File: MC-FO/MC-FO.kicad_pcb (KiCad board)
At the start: 4 copper layers, 160 x 100 mm, 93 parts, among them U101 74ACT08SCX, U102 IFE98, U121 74ACT08SCX, U122 IFE98, U141 IFD97, U142 TLV3501AID, U143 74LVC1G32SE-7, U161 IFD97, U163 74LVC1G32SE-7, U181 BU4831F-TR, U182 BU4847F-TR, U183 74ACT08SCX, U184 74LVC1G07QDCKTQ1, U2 R-78E3.3-0.5, U27 74ACT08SCX, U28 IFE98, U3 R-78E5.0-0.5, U41 74ACT08SCX, U42 IFE98, U61 74ACT08SCX, U62 IFE98, U81 74ACT08SCX, U82 IFE98

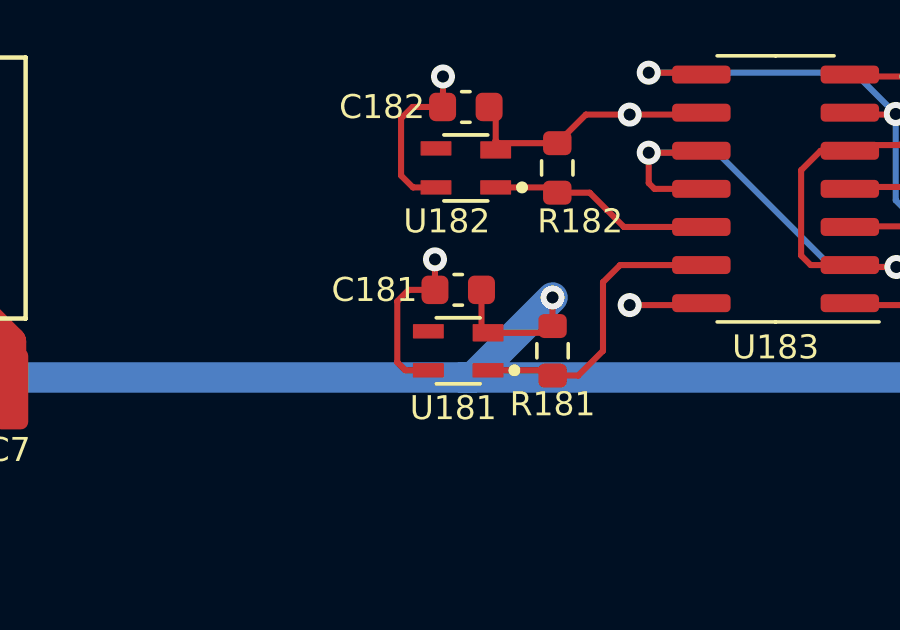
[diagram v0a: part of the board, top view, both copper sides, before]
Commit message: updated top level of schematic with "to test" and "to do" notes
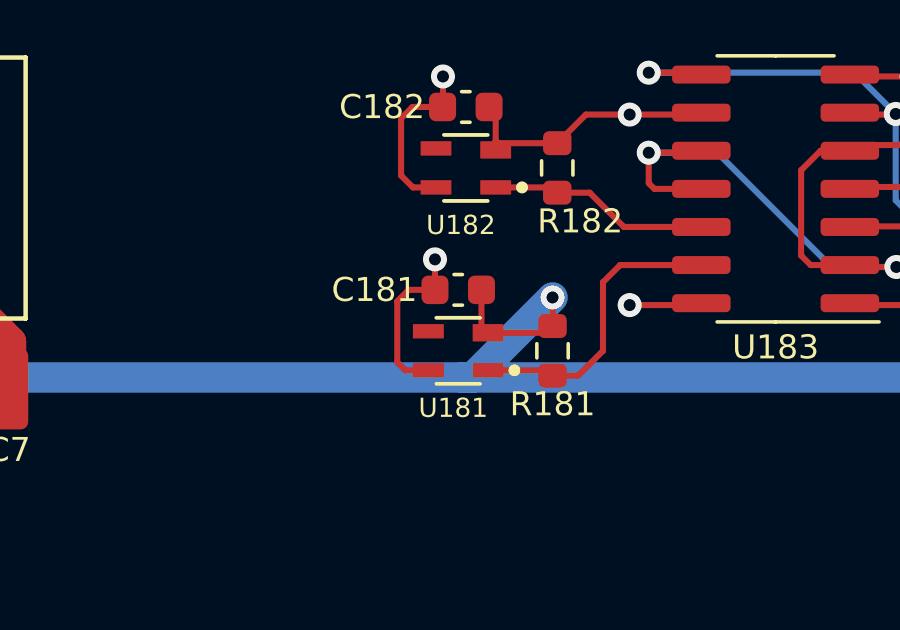
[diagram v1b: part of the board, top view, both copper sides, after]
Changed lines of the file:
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@@
   (general
     (thickness 1.6)
-    (drawings 20)
+    (drawings 30)
     (tracks 806)
     (zones 0)
@@
   (module BU4847F-TR:SOT130P210X105-4N (layer F.Cu)
     (at 168.275 66.802 180)
-    (fp_text reference U182 (at 0.635 -1.778) (layer F.SilkS)
-      (effects (font (size 0.8 0.8) (thickness 0.2)))
+    (fp_text reference U182 (at 0.167055 -1.907023) (layer F.SilkS)
+      (effects (font (size 0.640209 0.640209) (thickness 0.15)))
     )
-    (fp_text value BU4847F-TR (at 5.008681 1.881434) (layer F.Fab) hide
+    (fp_text value BU4847F-TR (at 5.008681 1.881434) (layer F.Fab)
       (effects (font (size 0.640624 0.640624) (thickness 0.15)))
     )
@@
     (at 168.021 72.898 180)
     (fp_text reference U181 (at 0.167055 -1.907023) (layer F.SilkS)
-      (effects (font (size 0.8 0.8) (thickness 0.2)))
+      (effects (font (size 0.640209 0.640209) (thickness 0.15)))
     )
-    (fp_text value BU4831F-TR (at 5.008681 1.881434) (layer F.Fab) hide
+    (fp_text value BU4831F-TR (at 5.008681 1.881434) (layer F.Fab)
       (effects (font (size 0.640624 0.640624) (thickness 0.15)))
     )
@@
     (pad 1 thru_hole circle (at 0 0 180) (size 1.445 1.445) (drill 0.889) (layers *.Cu *.Mask)
       (net 1 GND))
+    (model "C:/Program Files/KiCad/share/kicad/modules/LED_THT.pretty/LED_D2.0mm_W4.8mm_H2.5mm_FlatTop.kicad_mod"
+      (at (xyz 0 0 0))
+      (scale (xyz 1 1 1))
+      (rotate (xyz 0 0 0))
+    )
+    (model ${KISYS3DMOD}/LED_THT.3dshapes/LED_D5.0mm_Horizontal_O6.35mm_Z3.0mm.wrl
+      (offset (xyz 0 2.5 0))
+      (scale (xyz 1 1 1))
+      (rotate (xyz 0 0 90))
+    )
   )
   (module Capacitor_SMD:C_1210_3225Metric (layer F.Cu)
@@
     (pad 32 thru_hole circle (at 19.05 10.16 90) (size 1.55 1.55) (drill 1) (layers *.Cu *.Mask)
       (net 1 GND))
-    (model ${KISYS3DMOD}/Connector_DIN.3dshapes/DIN41612_C2_2x16_Male_Horizontal_THT.wrl
-      (at (xyz 0 0 0))
+    (model ${KISYS3DMOD}/Connector_Dsub.3dshapes/DSUB-25_Female_Horizontal_P2.77x2.84mm_EdgePinOffset7.70mm_Housed_MountingHolesOffset9.12mm.step
+      (offset (xyz -16.5 -10 0))
       (scale (xyz 1 1 1))
-      (rotate (xyz 0 0 0))
+      (rotate (xyz 0 0 180))
     )
   )
@@
     (pad 1 thru_hole circle (at 0 0 90) (size 1.1 1.1) (drill 0.7) (layers *.Cu *.Mask)
       (net 1 GND))
+    (model ${KIPRJMOD}/Footprints_MC-FO/FOport-IFE98-IFD97.STEP
+      (offset (xyz 1.9 -16.5 0))
+      (scale (xyz 1 1 1))
+      (rotate (xyz -90 0 -90))
+    )
   )
   (module Package_SO:SOIC-14_3.9x8.7mm_P1.27mm (layer F.Cu)
@@
     (pad 1 thru_hole circle (at 0 0 90) (size 1.1 1.1) (drill 0.7) (layers *.Cu *.Mask)
       (net 1 GND))
+    (model ${KIPRJMOD}/Footprints_MC-FO/FOport-IFE98-IFD97.STEP
+      (offset (xyz 1.9 -16.5 0))
+      (scale (xyz 1 1 1))
+      (rotate (xyz -90 0 -90))
+    )
   )
   (module Package_SO:SOIC-14_3.9x8.7mm_P1.27mm (layer F.Cu)
@@
     (pad MH2 np_thru_hole circle (at -0.635 2.54 90) (size 1.775 0) (drill 1.775) (layers *.Cu *.Mask))
     (pad MH3 np_thru_hole circle (at 4.445 2.54 90) (size 1.775 0) (drill 1.775) (layers *.Cu *.Mask))
+    (model ${KIPRJMOD}/Footprints_MC-FO/FOport-IFE98-IFD97.STEP
+      (offset (xyz 1.9 -16.5 0))
+      (scale (xyz 1 1 1))
+      (rotate (xyz -90 0 -90))
+    )
   )
   (module Package_SO:SOIC-14_3.9x8.7mm_P1.27mm (layer F.Cu)
@@
     (pad MH2 np_thru_hole circle (at -0.635 2.54 90) (size 1.775 0) (drill 1.775) (layers *.Cu *.Mask))
     (pad MH3 np_thru_hole circle (at 4.445 2.54 90) (size 1.775 0) (drill 1.775) (layers *.Cu *.Mask))
+    (model ${KIPRJMOD}/Footprints_MC-FO/FOport-IFE98-IFD97.STEP
+      (offset (xyz 1.9 -16.5 0))
+      (scale (xyz 1 1 1))
+      (rotate (xyz -90 0 -90))
+    )
   )
   (module Package_SO:SOIC-14_3.9x8.7mm_P1.27mm (layer F.Cu)
@@
     (pad MH2 np_thru_hole circle (at -0.635 2.54 90) (size 1.775 0) (drill 1.775) (layers *.Cu *.Mask))
     (pad MH3 np_thru_hole circle (at 4.445 2.54 90) (size 1.775 0) (drill 1.775) (layers *.Cu *.Mask))
+    (model ${KIPRJMOD}/Footprints_MC-FO/FOport-IFE98-IFD97.STEP
+      (offset (xyz 1.9 -16.5 0))
+      (scale (xyz 1 1 1))
+      (rotate (xyz -90 0 -90))
+    )
   )
   (module Package_SO:SOIC-14_3.9x8.7mm_P1.27mm (layer F.Cu)
@@
     (pad MH2 np_thru_hole circle (at -0.635 2.54 90) (size 1.775 0) (drill 1.775) (layers *.Cu *.Mask))
     (pad MH3 np_thru_hole circle (at 4.445 2.54 90) (size 1.775 0) (drill 1.775) (layers *.Cu *.Mask))
+    (model ${KIPRJMOD}/Footprints_MC-FO/FOport-IFE98-IFD97.STEP
+      (offset (xyz 1.9 -16.5 0))
+      (scale (xyz 1 1 1))
+      (rotate (xyz -90 0 -90))
+    )
   )
   (module Footprints_MC-FO:IFE98 locked (layer F.Cu)
@@
     (pad 1 thru_hole circle (at 0 0 90) (size 1.1 1.1) (drill 0.7) (layers *.Cu *.Mask)
       (net 4 /Detector1/5V))
+    (model ${KIPRJMOD}/Footprints_MC-FO/FOport-IFE98-IFD97.STEP
+      (offset (xyz 1.9 -16.5 0))
+      (scale (xyz 1 1 1))
+      (rotate (xyz -90 0 -90))
+    )
   )
   (module Package_SO:SOIC-8_3.9x4.9mm_P1.27mm (layer F.Cu)
@@
     (pad MH2 np_thru_hole circle (at -0.635 2.54 90) (size 1.775 0) (drill 1.775) (layers *.Cu *.Mask))
     (pad MH3 np_thru_hole circle (at 4.445 2.54 90) (size 1.775 0) (drill 1.775) (layers *.Cu *.Mask))
+    (model ${KIPRJMOD}/Footprints_MC-FO/FOport-IFE98-IFD97.STEP
+      (offset (xyz 1.9 -16.5 0))
+      (scale (xyz 1 1 1))
+      (rotate (xyz -90 0 -90))
+    )
   )
   (module Package_TO_SOT_SMD:SOT-353_SC-70-5 (layer F.Cu)
@@
     )
   )
+  (gr_line (start 211.582 100.965) (end 209.931 98.552) (layer Cmts.User) (width 0.15))
+  (gr_line (start 210.566 97.79) (end 210.82 98.806) (layer Cmts.User) (width 0.15))
+  (gr_line (start 212.217 98.425) (end 210.947 97.282) (layer Cmts.User) (width 0.15))
+  (gr_line (start 219.329 99.187) (end 217.17 97.155) (layer Cmts.User) (width 0.15))
+  (gr_line (start 218.313 97.663) (end 218.567 96.393) (layer Cmts.User) (width 0.15))
+  (gr_line (start 218.694 99.314) (end 219.202 100.076) (layer Cmts.User) (width 0.15))
+  (gr_line (start 218.567 101.219) (end 218.313 100.711) (layer Cmts.User) (width 0.15))
+  (gr_line (start 220.726 101.092) (end 217.424 99.822) (layer Cmts.User) (width 0.15))
+  (gr_line (start 217.297 102.743) (end 220.726 102.743) (layer Cmts.User) (width 0.15))
+  (gr_line (start 216.662 101.727) (end 218.059 101.854) (layer Cmts.User) (width 0.15))
   (gr_text "EPWMA1\n" (at 224.608 78.451571) (layer B.SilkS)
     (effects (font (size 1 1) (thickness 0.15)))

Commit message: Add files via upload
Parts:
- removed C144: 0.1 uF, Capacitor_SMD:C_0603_1608Metric
- removed R144: 47K, Resistor_SMD:R_0603_1608Metric
- removed U143, U163: 74LVC1G32SE-7, Package_TO_SOT_SMD:SOT-353_SC-70-5
- added U162: 74LVC1G02SE-7, Package_TO_SOT_SMD:SOT-353_SC-70-5, F.Cu at (221.4, 142.1)
- R142: value 1K -> 47K
- U142: value TLV3501AID -> 74LVC1G02SE-7; footprint Package_SO:SOIC-8_3.9x4.9mm_P1.27mm -> Package_TO_SOT_SMD:SOT-353_SC-70-5
- U181, U182: footprint BU4847F-TR:SOT130P210X105-4N -> Package_SO:SOP-4_3.8x4.1mm_P2.54mm
- moved R143 59.7 mm to (263.7, 100.4)
- moved R141 53.7 mm to (275.3, 100.1), turned to 90 degrees
- moved R142 52.0 mm to (273.6, 100.1), turned to 90 degrees
- moved U142 51.5 mm to (266.3, 100.3), turned to 270 degrees
- moved C143 49.6 mm to (268.9, 100.2), turned to 90 degrees
- moved C141 47.4 mm to (279.5, 100.3), turned to 90 degrees
- moved C142 47.0 mm to (279.1, 97.3), turned to 270 degrees
- moved R161 4.27 mm to (229.4, 144.0), turned to 90 degrees
- moved C161 3.00 mm to (231.5, 141.2)
- moved C162 3.00 mm to (231.5, 138.4)
- moved R162 1.74 mm to (227.3, 143.2), turned to 0 degrees
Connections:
- C101 pad 1: /Detector1/5V -> /Emitter1/5V
- C102 pad 1: /Detector1/5V -> /Emitter1/5V
- C103 pad 1: /Detector1/5V -> /Emitter1/5V
- C121 pad 1: /Detector1/5V -> /Emitter1/5V
- C122 pad 1: /Detector1/5V -> /Emitter1/5V
- C123 pad 1: /Detector1/5V -> /Emitter1/5V
- C141 pad 1: /Detector1/5V -> /Emitter1/5V
- C141 pad 2: GND -> Net-(C141-Pad2)
- C142 pad 1: /Detector1/5V -> /Emitter1/5V
- C142 pad 2: GND -> Net-(C141-Pad2)
- C143 pad 1: /Detector1/5V -> VCC
- C143 pad 2: GND -> Net-(C141-Pad2)
- C161 pad 1: /Detector1/5V -> /Emitter1/5V
- C162 pad 1: /Detector1/5V -> /Emitter1/5V
- C182 pad 1: /Detector1/5V -> /Emitter1/5V
- C33 pad 1: /Detector1/5V -> /Emitter1/5V
- C34 pad 1: /Detector1/5V -> /Emitter1/5V
- C35 pad 1: /Detector1/5V -> /Emitter1/5V
- C41 pad 1: /Detector1/5V -> /Emitter1/5V
- C42 pad 1: /Detector1/5V -> /Emitter1/5V
- C43 pad 1: /Detector1/5V -> /Emitter1/5V
- C61 pad 1: /Detector1/5V -> /Emitter1/5V
- C62 pad 1: /Detector1/5V -> /Emitter1/5V
- C63 pad 1: /Detector1/5V -> /Emitter1/5V
- C7 pad 1: /Detector1/5V -> /Emitter1/5V
- C81 pad 1: /Detector1/5V -> /Emitter1/5V
- C82 pad 1: /Detector1/5V -> /Emitter1/5V
- C83 pad 1: /Detector1/5V -> /Emitter1/5V
- R102 pad 2: /Detector1/5V -> /Emitter1/5V
- R122 pad 2: /Detector1/5V -> /Emitter1/5V
- R141 pad 2: /Detector1/5V -> Net-(R141-Pad2)
- R142 pad 1: GND -> STATUS1
- R142 pad 2: Net-(R141-Pad1) -> Net-(R141-Pad2)
- R182 pad 1: /Detector1/5V -> /Emitter1/5V
- R28 pad 2: /Detector1/5V -> /Emitter1/5V
- R42 pad 2: /Detector1/5V -> /Emitter1/5V
- R62 pad 2: /Detector1/5V -> /Emitter1/5V
- R82 pad 2: /Detector1/5V -> /Emitter1/5V
- U101 pad 1: /Detector1/5V -> /Emitter1/5V
- U101 pad 14: /Detector1/5V -> /Emitter1/5V
- U101 pad 5: /Detector1/5V -> /Emitter1/5V
- U101 pad 9: /Detector1/5V -> /Emitter1/5V
- U121 pad 1: /Detector1/5V -> /Emitter1/5V
- U121 pad 14: /Detector1/5V -> /Emitter1/5V
- U121 pad 5: /Detector1/5V -> /Emitter1/5V
- U121 pad 9: /Detector1/5V -> /Emitter1/5V
- U141 pad 1: /Detector1/5V -> GND
- U141 pad 2: GND -> Net-(R141-Pad1)
- U141 pad 3: Net-(U141-Pad3) -> GND
- U141 pad 4: GND -> /Emitter1/5V
- U142 pad 1: Net-(R141-Pad1) -> Net-(R141-Pad2)
- U142 pad 3: Net-(U141-Pad3) -> GND
- U142 pad 4: /Detector1/5V -> STATUS1
- U142 pad 5: Net-(R144-Pad2) -> VCC
- U161 pad 1: /Detector1/5V -> GND
- U161 pad 2: GND -> Net-(R161-Pad1)
- U161 pad 3: Net-(R161-Pad1) -> GND
- U161 pad 4: GND -> /Emitter1/5V
- U182 pad 2: /Detector1/5V -> /Emitter1/5V
- U183 pad 1: /Detector1/5V -> /Emitter1/5V
- U183 pad 14: /Detector1/5V -> /Emitter1/5V
- U183 pad 4: /Detector1/5V -> /Emitter1/5V
- U183 pad 9: /Detector1/5V -> /Emitter1/5V
- U27 pad 1: /Detector1/5V -> /Emitter1/5V
- U27 pad 14: /Detector1/5V -> /Emitter1/5V
- U27 pad 5: /Detector1/5V -> /Emitter1/5V
- U27 pad 9: /Detector1/5V -> /Emitter1/5V
- U3 pad 3: /Detector1/5V -> /Emitter1/5V
- U41 pad 1: /Detector1/5V -> /Emitter1/5V
- U41 pad 14: /Detector1/5V -> /Emitter1/5V
- U41 pad 5: /Detector1/5V -> /Emitter1/5V
- U41 pad 9: /Detector1/5V -> /Emitter1/5V
- U61 pad 1: /Detector1/5V -> /Emitter1/5V
- U61 pad 14: /Detector1/5V -> /Emitter1/5V
- U61 pad 5: /Detector1/5V -> /Emitter1/5V
- U61 pad 9: /Detector1/5V -> /Emitter1/5V
- U81 pad 1: /Detector1/5V -> /Emitter1/5V
- U81 pad 14: /Detector1/5V -> /Emitter1/5V
- U81 pad 5: /Detector1/5V -> /Emitter1/5V
- U81 pad 9: /Detector1/5V -> /Emitter1/5V
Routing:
- net /Detector1/5V: track 147.6 -> 2.06 mm, vias 37 -> 2
- net /Emitter1/5V: track 0.00 -> 134.4 mm, vias 0 -> 34
- net Net-(U141-Pad3): track 26.0 -> 0.00 mm
- net Net-(R144-Pad2): track 13.0 -> 0.00 mm
- net GND: track 105.9 -> 93.5 mm, vias 30 -> 28
- net VCC: track 202.4 -> 196.8 mm
- net Net-(R141-Pad1): track 6.84 -> 2.92 mm
- net Net-(R161-Pad2): track 6.49 -> 8.62 mm
- net STATUS2: track 142.3 -> 140.2 mm
- net Net-(R161-Pad1): track 13.9 -> 15.4 mm

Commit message: schematic changes--> layout rev
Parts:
- removed R141, R161: 2.4K, Resistor_SMD:R_0603_1608Metric
- removed R142, R162: 47K, Resistor_SMD:R_0603_1608Metric
- removed R143, R163: 10K, Resistor_SMD:R_0603_1608Metric
- removed the U183 at (178.6, 67.5)
- removed the U184 at (185.6, 64.3)
- added R11: 10K, Resistor_SMD:R_0603_1608Metric, F.Cu at (99.5, 114.5)
- added TP1: TestPoint, TestPoint:TestPoint_Pad_D2.0mm, F.Cu at (105.1, 77.7)
- added TP101: TestPoint, TestPoint:TestPoint_Pad_D2.0mm, F.Cu at (169.2, 118.5)
- added TP11: TestPoint, TestPoint:TestPoint_Pad_D2.0mm, F.Cu at (130.7, 102.8)
- added TP12: TestPoint, TestPoint:TestPoint_Pad_D2.0mm, F.Cu at (145.2, 52.7)
- added TP121: TestPoint, TestPoint:TestPoint_Pad_D2.0mm, F.Cu at (152.8, 117.5)
- added TP13: TestPoint, TestPoint:TestPoint_Pad_D2.0mm, F.Cu at (128.4, 42.9)
- added TP14: TestPoint, TestPoint:TestPoint_Pad_D2.0mm, F.Cu at (116.9, 102.2)
- added TP141: TestPoint, TestPoint:TestPoint_Pad_D2.0mm, F.Cu at (170.4, 98.9)
- added TP161: TestPoint, TestPoint:TestPoint_Pad_D2.0mm, F.Cu at (166.4, 143.0)
- added TP181: TestPoint, TestPoint:TestPoint_Pad_D2.0mm, F.Cu at (169.4, 36.8)
- added TP182: TestPoint, TestPoint:TestPoint_Pad_D2.0mm, F.Cu at (156.2, 39.8)
- added TP183: TestPoint, TestPoint:TestPoint_Pad_D2.0mm, F.Cu at (173.8, 27.3)
- added TP21: TestPoint, TestPoint:TestPoint_Pad_D2.0mm, F.Cu at (145.4, 84.3)
- added TP41: TestPoint, TestPoint:TestPoint_Pad_D2.0mm, F.Cu at (152.3, 89.3)
- added TP61: TestPoint, TestPoint:TestPoint_Pad_D2.0mm, F.Cu at (159.7, 93.3)
- added TP81: TestPoint, TestPoint:TestPoint_Pad_D2.0mm, F.Cu at (173.9, 104.5)
- added U11: 74LVCE1G08W5-7, Package_TO_SOT_SMD:SOT-23-5_HandSoldering, F.Cu at (124.4, 102.3)
- added U181: 74LVC1G07QDCKTQ1, Package_TO_SOT_SMD:SOT-353_SC-70-5_Handsoldering, F.Cu at (185.6, 64.3)
- added U182: 74LVCE1G08W5-7, Package_TO_SOT_SMD:SOT-23-5_HandSoldering, F.Cu at (177.5, 55.5)
- U141, U161: footprint Footprints_MC-FO:IFE98 -> Footprints_MC-FO:IFD97
- U142, U162: footprint Package_TO_SOT_SMD:SOT-353_SC-70-5 -> Package_TO_SOT_SMD:SOT-353_SC-70-5_Handsoldering
- moved C142 48.9 mm to (230.3, 97.5)
- moved C141 47.9 mm to (231.7, 97.5), turned to 270 degrees
- moved R183 45.4 mm to (157.5, 33.0), turned to 0 degrees
- moved C143 42.9 mm to (226.0, 102.6), turned to 180 degrees
- moved U142 36.4 mm to (229.9, 102.0), turned to 180 degrees
- moved U162 8.74 mm to (229.9, 143.8), turned to 180 degrees
- moved C163 6.52 mm to (229.0, 146.0), turned to 0 degrees
- moved C161 2.12 mm to (230.2, 139.5)
- moved C162 1.11 mm to (231.6, 139.5), turned to 270 degrees
- renumbered C182 to C181, C181 to C182, C33 to C21, C34 to C22, C35 to C23, C36 to C24, R184 to R182, R181 to R184, R182 to R185, R29 to R21, R27 to R22, R28 to R23, U181 to U183, U182 to U184, U27 to U21, U28 to U22
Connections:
- C101 pad 1: /Emitter1/5V -> /Detector1/5V
- C102 pad 1: /Emitter1/5V -> /Detector1/5V
- C103 pad 1: /Emitter1/5V -> /Detector1/5V
- C121 pad 1: /Emitter1/5V -> /Detector1/5V
- C122 pad 1: /Emitter1/5V -> /Detector1/5V
- C123 pad 1: /Emitter1/5V -> /Detector1/5V
- C141 pad 1: /Emitter1/5V -> /Detector1/5V
- C141 pad 2: Net-(C141-Pad2) -> GND
- C142 pad 1: /Emitter1/5V -> /Detector1/5V
- C142 pad 2: Net-(C141-Pad2) -> GND
- C143 pad 1: VCC -> /Detector1/3V3
- C143 pad 2: Net-(C141-Pad2) -> GND
- C161 pad 1: /Emitter1/5V -> /Detector1/5V
- C162 pad 1: /Emitter1/5V -> /Detector1/5V
- C163 pad 1: VCC -> /Detector1/3V3
- C181 pad 1: /Emitter1/5V -> /Detector1/5V
- C182 pad 1: VCC -> /Detector1/3V3
- C21 pad 1: /Emitter1/5V -> /Detector1/5V
- C22 pad 1: /Emitter1/5V -> /Detector1/5V
- C23 pad 1: /Emitter1/5V -> /Detector1/5V
- C41 pad 1: /Emitter1/5V -> /Detector1/5V
- C42 pad 1: /Emitter1/5V -> /Detector1/5V
- C43 pad 1: /Emitter1/5V -> /Detector1/5V
- C6 pad 1: VCC -> /Detector1/3V3
- C61 pad 1: /Emitter1/5V -> /Detector1/5V
- C62 pad 1: /Emitter1/5V -> /Detector1/5V
- C63 pad 1: /Emitter1/5V -> /Detector1/5V
- C7 pad 1: /Emitter1/5V -> /Detector1/5V
- C81 pad 1: /Emitter1/5V -> /Detector1/5V
- C82 pad 1: /Emitter1/5V -> /Detector1/5V
- C83 pad 1: /Emitter1/5V -> /Detector1/5V
- H1 pad 17: STATUS2 -> GND
- H1 pad 19: RESET2 -> GND
- H1 pad 2: GND -> ~SAFE_STATE_FLAG~
- H1 pad 21: EPWM2B -> STATUS2
- H1 pad 23: EPWM2A -> EPWM2B
- H1 pad 25: STATUS1 -> EPWM2A
- H1 pad 27: RESET1 -> STATUS1
- H1 pad 4: GND -> EMITTER_ENABLE
- H1 pad 6: GND -> RESET_GPIO
- R102 pad 2: /Emitter1/5V -> /Detector1/5V
- R122 pad 2: /Emitter1/5V -> /Detector1/5V
- R123 pad 2: RESET2 -> RESET_GPIO
- R182 pad 1: VCC -> /Detector1/3V3
- R182 pad 2: /Emitter1/RESET_FO -> ~SAFE_STATE_FLAG~
- R184 pad 1: VCC -> /Detector1/5V
- R185 pad 1: /Emitter1/5V -> /Detector1/5V
- R23 pad 2: /Emitter1/5V -> /Detector1/5V
- R42 pad 2: /Emitter1/5V -> /Detector1/5V
- R62 pad 2: /Emitter1/5V -> /Detector1/5V
- R63 pad 2: RESET1 -> RESET_GPIO
- R82 pad 2: /Emitter1/5V -> /Detector1/5V
- U101 pad 1: /Emitter1/5V -> /Detector1/5V
- U101 pad 14: /Emitter1/5V -> /Detector1/5V
- U101 pad 5: /Emitter1/5V -> /Detector1/5V
- U101 pad 9: /Emitter1/5V -> /Detector1/5V
- U121 pad 1: /Emitter1/5V -> /Detector1/5V
- U121 pad 12: RESET2 -> RESET_GPIO
- U121 pad 14: /Emitter1/5V -> /Detector1/5V
- U121 pad 5: /Emitter1/5V -> /Detector1/5V
- U121 pad 9: /Emitter1/5V -> /Detector1/5V
- U141 pad 2: Net-(R141-Pad1) -> Net-(U141-Pad2)
- U141 pad 4: /Emitter1/5V -> /Detector1/5V
- U142 pad 1: Net-(R141-Pad2) -> Net-(U141-Pad2)
- U142 pad 5: VCC -> /Detector1/3V3
- U161 pad 2: Net-(R161-Pad1) -> Net-(U161-Pad2)
- U161 pad 4: /Emitter1/5V -> /Detector1/5V
- U162 pad 1: Net-(R161-Pad2) -> Net-(U161-Pad2)
- U162 pad 5: VCC -> /Detector1/3V3
- U183 pad 2: VCC -> /Detector1/3V3
- U184 pad 2: /Emitter1/5V -> /Detector1/5V
- U2 pad 3: VCC -> /Detector1/3V3
- U21 pad 1: /Emitter1/5V -> /Detector1/5V
- U21 pad 14: /Emitter1/5V -> /Detector1/5V
- U21 pad 5: /Emitter1/5V -> /Detector1/5V
- U21 pad 9: /Emitter1/5V -> /Detector1/5V
- U3 pad 3: /Emitter1/5V -> /Detector1/5V
- U41 pad 1: /Emitter1/5V -> /Detector1/5V
- U41 pad 14: /Emitter1/5V -> /Detector1/5V
- U41 pad 5: /Emitter1/5V -> /Detector1/5V
- U41 pad 9: /Emitter1/5V -> /Detector1/5V
- U61 pad 1: /Emitter1/5V -> /Detector1/5V
- U61 pad 12: RESET1 -> RESET_GPIO
- U61 pad 14: /Emitter1/5V -> /Detector1/5V
- U61 pad 5: /Emitter1/5V -> /Detector1/5V
- U61 pad 9: /Emitter1/5V -> /Detector1/5V
- U81 pad 1: /Emitter1/5V -> /Detector1/5V
- U81 pad 14: /Emitter1/5V -> /Detector1/5V
- U81 pad 5: /Emitter1/5V -> /Detector1/5V
- U81 pad 9: /Emitter1/5V -> /Detector1/5V
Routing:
- net RESET_GPIO: track 0.00 -> 258.9 mm
- net /Emitter1/5V: track 134.4 -> 0.00 mm, vias 34 -> 0
- net /Detector1/5V: track 2.06 -> 132.1 mm, vias 2 -> 34
- net RESET2: track 119.9 -> 0.00 mm
- net RESET1: track 114.5 -> 0.00 mm
- net Net-(U183-Pad10): track 28.5 -> 0.00 mm, vias 2 -> 0
- net Net-(R183-Pad2): track 21.3 -> 49.8 mm, vias 3 -> 5
- net STATUS1: track 109.3 -> 134.8 mm
- net Net-(R161-Pad1): track 15.4 -> 0.00 mm
- net Net-(U141-Pad2): track 0.00 -> 11.0 mm
- net Net-(U161-Pad2): track 0.00 -> 10.9 mm
- net VCC: track 196.8 -> 187.3 mm, vias 5 -> 2
- net EMITTER_ENABLE: track 0.00 -> 8.69 mm
- net Net-(R161-Pad2): track 8.62 -> 0.00 mm
- net STATUS2: track 140.2 -> 145.8 mm
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
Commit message: Pre final revision Layout
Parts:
- moved R11 89.9 mm to (182.1, 78.9), turned to 180 degrees
- moved TP11 64.9 mm to (187.7, 71.8)
- moved U11 62.8 mm to (181.3, 75.7), turned to 90 degrees
- moved TP21 53.9 mm to (197.1, 69.1)
- moved TP14 53.6 mm to (166.8, 82.7)
- moved R183 48.1 mm to (197.1, 60.3), turned to 180 degrees
- moved TP181 42.1 mm to (175.8, 78.5)
- moved TP121 39.4 mm to (189.3, 132.3)
- moved TP183 39.1 mm to (175.5, 66.4)
- moved TP41 38.7 mm to (189.8, 79.6)
- moved TP182 37.6 mm to (176.0, 71.8)
- moved TP61 29.6 mm to (189.2, 90.1)
- moved TP13 28.7 mm to (134.8, 70.9)
- moved TP161 23.3 mm to (189.4, 139.4)
- moved TP101 20.3 mm to (189.3, 121.7)
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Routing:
- net /Detector1/3V3: track 3.51 -> 224.7 mm, vias 0 -> 5
- net VCC: track 187.3 -> 0.00 mm, vias 2 -> 0
- net ~SAFE_STATE_FLAG~: track 0.00 -> 129.2 mm, vias 0 -> 1
- net EMITTER_ENABLE: track 8.69 -> 105.7 mm, vias 0 -> 1
- net Net-(R183-Pad2): track 49.8 -> 19.2 mm, vias 5 -> 0
- net Net-(D181-Pad2): track 59.5 -> 44.5 mm
- net /Emitter1/RESET_FO: track 139.6 -> 147.7 mm
- net GND: track 91.0 -> 97.4 mm, vias 25 -> 28
- net RESET_GPIO: track 258.9 -> 253.0 mm, vias 0 -> 1
- net /Detector1/5V: track 132.1 -> 137.4 mm, vias 34 -> 36
- net EPWM1A: track 119.0 -> 121.7 mm
- net Net-(R185-Pad2): track 7.40 -> 9.03 mm
- net Net-(R184-Pad2): track 10.0 -> 10.8 mm
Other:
- board text added: "EPWM1A"
- board text added: "EPWM1B"
- board text added: "EPWM2A"
- board text added: "EPWM2B"
- board text added: "RESET_GPIO"
- board text added: "STATUS1"
- board text added: "STATUS2"
- board text removed: "EPWMA2"
- board text removed: "EPWMB1"
- board text removed: "EPWMB2"
- board text removed: "Reset1"
- board text removed: "Reset2"
- board text removed: "Status2"
